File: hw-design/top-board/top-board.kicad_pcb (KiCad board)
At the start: 2 copper layers, 170 x 65.9 mm, 115 parts, among them P1 POWER_CONN, P2 BACKLIGHT, P3 BACKLIGHT, P4 BOTTOM_CONN, P5 ISP, P6 SPI_JTAG, P7 FOOTSWITCH, P8 FOOTSWITCH, Q1 2N7002, Q2 2N7002, SW1 SW_PUSH, U1 NCP1117DT33G, U2 74AHC1G00, U3 LPC1759FBD80, U4 PCA9685, Y1 10MHz

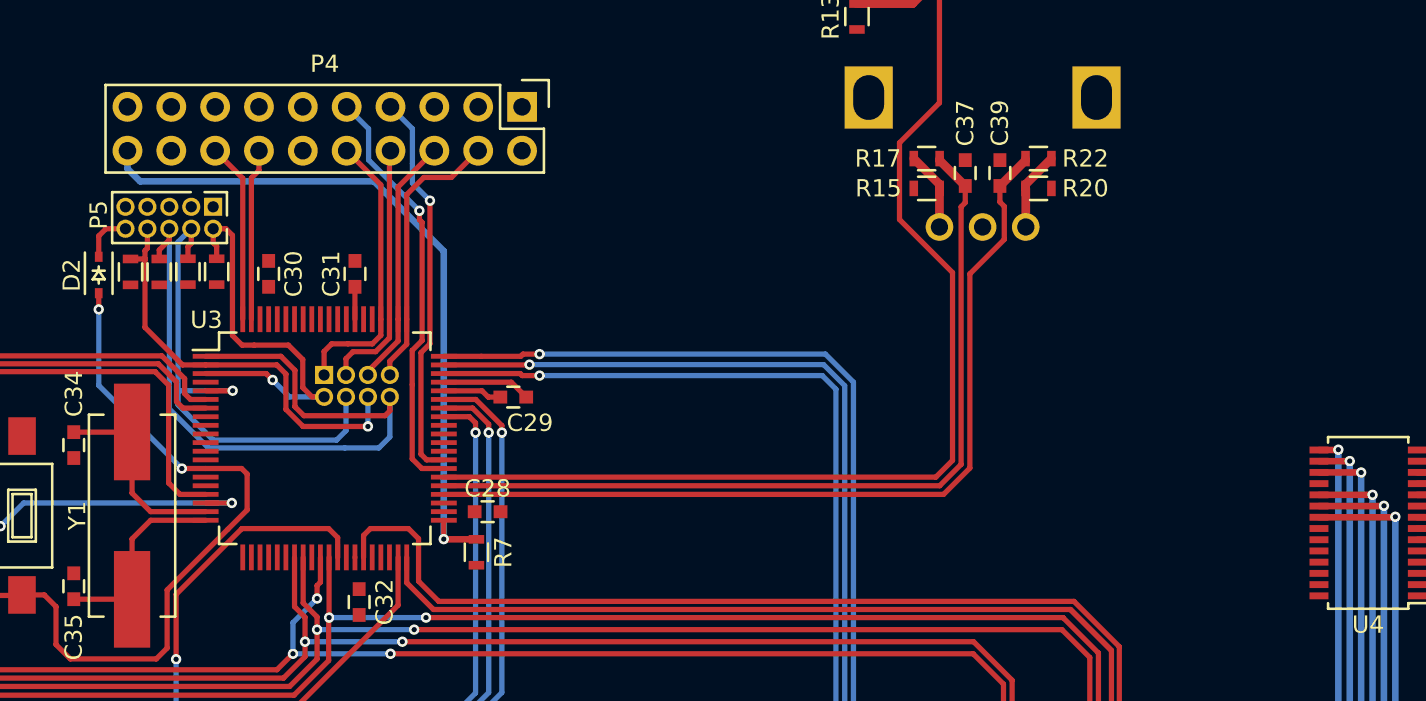
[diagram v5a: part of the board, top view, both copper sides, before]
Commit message: pcb,top-board: PCA interface signals traced
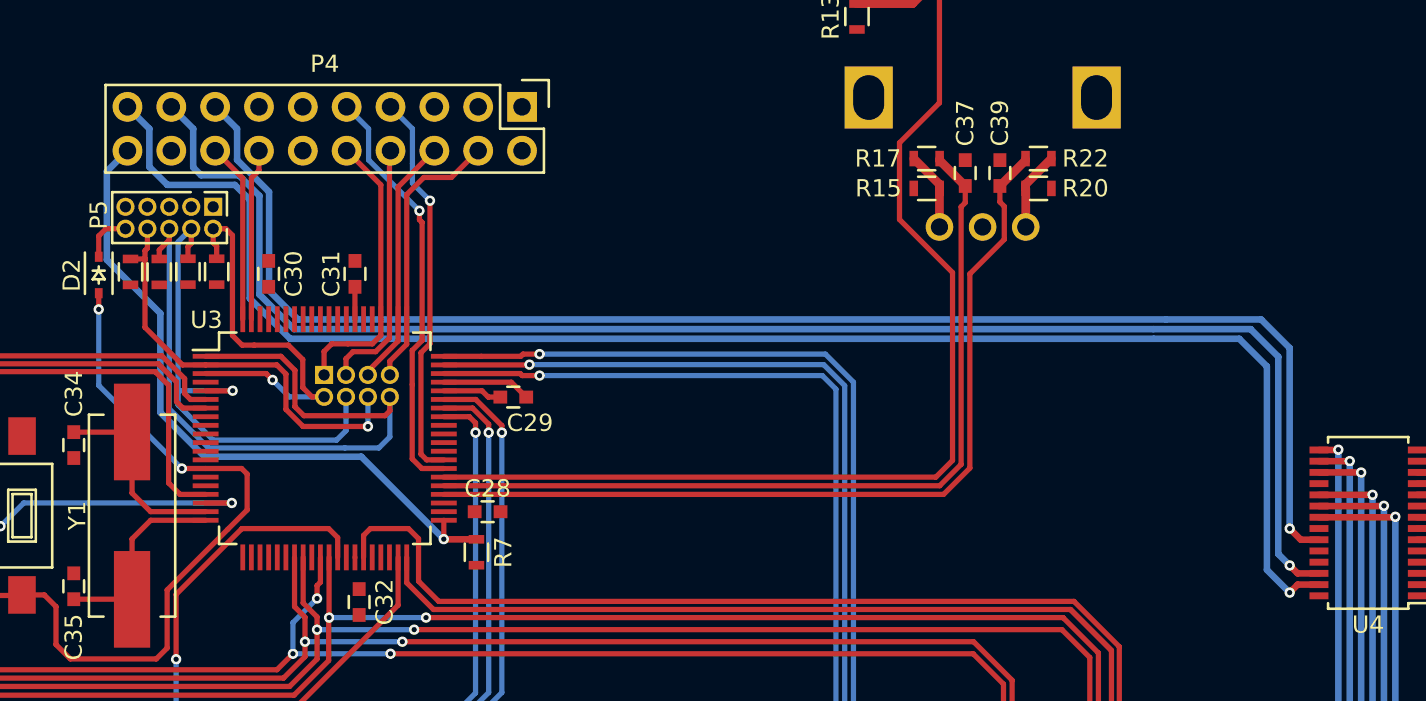
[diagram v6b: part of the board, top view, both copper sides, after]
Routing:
- net PM_LEDS_SDA: track 0.00 -> 92.4 mm, vias 0 -> 1
- net PM_LEDS_SCL: track 0.00 -> 89.0 mm, vias 0 -> 1
- net PM_LEDS_OE: track 0.00 -> 84.9 mm, vias 0 -> 1
- net HMI_ISP_ENABLE: track 41.0 -> 39.4 mm
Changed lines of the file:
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@@
   (general
     (links 318)
-    (no_connects 163)
+    (no_connects 160)
     (area 71.624905 39.007697 241.724909 105.045908)
     (thickness 1.6)
     (drawings 9)
-    (tracks 709)
+    (tracks 753)
     (zones 0)
     (modules 115)
@@
   )
   (setup
-    (last_trace_width 0.3048)
+    (last_trace_width 0.381)
     (user_trace_width 0.2032)
     (user_trace_width 0.254)
@@
   (gr_line (start 241.674908 39.057698) (end 71.674906 39.057698) (layer Edge.Cuts) (width 0.1))
   (gr_line (start 71.674906 104.995907) (end 241.674908 104.995907) (layer Edge.Cuts) (width 0.1))
-  (segment (start 163.5926 64.7204) (end 167.5022 64.7204) (width 0.3048) (layer F.Cu) (net 2) (status 400000))
-  (segment (start 167.5022 64.7204) (end 168.3646 65.5828) (width 0.3048) (layer F.Cu) (net 2) (status 800000))
-  (segment (start 166.8646 65.5828) (end 166.1668 65.5828) (width 0.3048) (layer F.Cu) (net 3) (status 400000))
+  (segment (start 163.5926 64.7204) (end 167.5022 64.7204) (width 0.3048) (layer F.Cu) (net 2))
+  (segment (start 167.5022 64.7204) (end 168.3646 65.5828) (width 0.3048) (layer F.Cu) (net 2))
+  (segment (start 166.8646 65.5828) (end 166.1668 65.5828) (width 0.3048) (layer F.Cu) (net 3))
   (segment (start 166.1668 65.5828) (end 165.8044 65.2204) (width 0.3048) (layer F.Cu) (net 3))
-  (segment (start 163.5926 65.2204) (end 165.8044 65.2204) (width 0.3048) (layer F.Cu) (net 3) (status 400000))
+  (segment (start 163.5926 65.2204) (end 165.8044 65.2204) (width 0.3048) (layer F.Cu) (net 3))
   (segment (start 158.4426 59.198) (end 158.4452 59.1954) (width 0.3048) (layer F.Cu) (net 3))
   (segment (start 158.4426 61.0704) (end 158.4426 59.198) (width 0.3048) (layer F.Cu) (net 3))
@@
   (segment (start 152.8826 52.451) (end 152.8826 51.308) (width 0.3048) (layer F.Cu) (net 78))
   (segment (start 152.4426 61.0704) (end 152.4426 52.891) (width 0.3048) (layer F.Cu) (net 78))
+  (segment (start 214.2946 73.8476) (end 213.2428 73.8476) (width 0.381) (layer F.Cu) (net 79) (status 400000))
+  (segment (start 210.947 61.087) (end 205.4352 61.087) (width 0.381) (layer B.Cu) (net 79))
+  (segment (start 212.598 62.738) (end 210.947 61.087) (width 0.381) (layer B.Cu) (net 79))
+  (segment (start 212.598 73.2028) (end 212.598 62.738) (width 0.381) (layer B.Cu) (net 79))
+  (via (at 212.598 73.2028) (size 0.6) (layers F.Cu B.Cu) (net 79))
+  (segment (start 213.2428 73.8476) (end 212.598 73.2028) (width 0.381) (layer F.Cu) (net 79))
+  (segment (start 150.3426 48.768) (end 151.6126 50.038) (width 0.381) (layer B.Cu) (net 79) (status 400000))
+  (segment (start 155.1432 61.087) (end 205.4352 61.087) (width 0.381) (layer B.Cu) (net 79))
+  (segment (start 153.4668 59.4106) (end 155.1432 61.087) (width 0.381) (layer B.Cu) (net 79))
+  (segment (start 153.4668 53.6956) (end 153.4668 59.4106) (width 0.381) (layer B.Cu) (net 79))
+  (segment (start 151.6126 51.8414) (end 153.4668 53.6956) (width 0.381) (layer B.Cu) (net 79))
+  (segment (start 151.6126 50.038) (end 151.6126 51.8414) (width 0.381) (layer B.Cu) (net 79))
   (segment (start 151.9426 52.908) (end 150.3426 51.308) (width 0.3048) (layer F.Cu) (net 80))
   (segment (start 151.9426 61.0704) (end 151.9426 52.908) (width 0.3048) (layer F.Cu) (net 80))
-  (segment (start 145.2626 52.3494) (end 145.9992 53.086) (width 0.381) (layer B.Cu) (net 84))
-  (segment (start 145.9992 53.086) (end 159.5501 53.086) (width 0.381) (layer B.Cu) (net 84))
-  (segment (start 159.5501 53.086) (end 163.5887 57.1246) (width 0.381) (layer B.Cu) (net 84))
-  (segment (start 163.5887 57.1246) (end 163.5887 73.8124) (width 0.381) (layer B.Cu) (net 84))
+  (segment (start 214.2946 75.7976) (end 213.0592 75.7976) (width 0.381) (layer F.Cu) (net 81) (status 400000))
+  (segment (start 210.3374 61.6458) (end 204.6986 61.6458) (width 0.381) (layer B.Cu) (net 81))
+  (segment (start 211.9376 63.246) (end 210.3374 61.6458) (width 0.381) (layer B.Cu) (net 81))
+  (segment (start 211.9376 74.676) (end 211.9376 63.246) (width 0.381) (layer B.Cu) (net 81))
+  (segment (start 212.598 75.3364) (end 211.9376 74.676) (width 0.381) (layer B.Cu) (net 81))
+  (via (at 212.598 75.3364) (size 0.6) (layers F.Cu B.Cu) (net 81))
+  (segment (start 213.0592 75.7976) (end 212.598 75.3364) (width 0.381) (layer F.Cu) (net 81))
+  (segment (start 147.8026 48.768) (end 149.0726 50.038) (width 0.381) (layer B.Cu) (net 81) (status 400000))
+  (segment (start 154.9146 61.6458) (end 204.6986 61.6458) (width 0.381) (layer B.Cu) (net 81))
+  (segment (start 152.908 59.6392) (end 154.9146 61.6458) (width 0.381) (layer B.Cu) (net 81))
+  (segment (start 152.908 53.9242) (end 152.908 59.6392) (width 0.381) (layer B.Cu) (net 81))
+  (segment (start 151.7142 52.7304) (end 152.908 53.9242) (width 0.381) (layer B.Cu) (net 81))
+  (segment (start 149.527402 52.7304) (end 151.7142 52.7304) (width 0.381) (layer B.Cu) (net 81))
+  (segment (start 149.0726 52.275598) (end 149.527402 52.7304) (width 0.381) (layer B.Cu) (net 81))
+  (segment (start 149.0726 50.038) (end 149.0726 52.275598) (width 0.381) (layer B.Cu) (net 81))
+  (segment (start 214.2946 76.4476) (end 213.0616 76.4476) (width 0.381) (layer F.Cu) (net 83) (status 400000))
+  (segment (start 209.677 62.2046) (end 204.724 62.2046) (width 0.381) (layer B.Cu) (net 83))
+  (segment (start 211.2772 63.8048) (end 209.677 62.2046) (width 0.381) (layer B.Cu) (net 83))
+  (segment (start 211.2772 75.5904) (end 211.2772 63.8048) (width 0.381) (layer B.Cu) (net 83))
+  (segment (start 212.598 76.9112) (end 211.2772 75.5904) (width 0.381) (layer B.Cu) (net 83))
+  (via (at 212.598 76.9112) (size 0.6) (layers F.Cu B.Cu) (net 83))
+  (segment (start 213.0616 76.4476) (end 212.598 76.9112) (width 0.381) (layer F.Cu) (net 83))
+  (segment (start 145.2626 48.768) (end 146.5326 50.038) (width 0.381) (layer B.Cu) (net 83) (status 400000))
+  (segment (start 154.686 62.2046) (end 204.724 62.2046) (width 0.381) (layer B.Cu) (net 83))
+  (segment (start 152.3492 59.8678) (end 154.686 62.2046) (width 0.381) (layer B.Cu) (net 83))
+  (segment (start 152.3492 54.1528) (end 152.3492 59.8678) (width 0.381) (layer B.Cu) (net 83))
+  (segment (start 151.4856 53.2892) (end 152.3492 54.1528) (width 0.381) (layer B.Cu) (net 83))
+  (segment (start 147.574 53.2892) (end 151.4856 53.2892) (width 0.381) (layer B.Cu) (net 83))
+  (segment (start 146.5326 52.2478) (end 147.574 53.2892) (width 0.381) (layer B.Cu) (net 83))
+  (segment (start 146.5326 50.038) (end 146.5326 52.2478) (width 0.381) (layer B.Cu) (net 83))
+  (segment (start 145.2626 51.308) (end 144.0688 52.5018) (width 0.381) (layer B.Cu) (net 84) (status 400000))
+  (segment (start 158.8135 69.0372) (end 163.5887 73.8124) (width 0.381) (layer B.Cu) (net 84))
+  (segment (start 149.733 69.0372) (end 158.8135 69.0372) (width 0.381) (layer B.Cu) (net 84))
+  (segment (start 147.1676 66.4718) (end 149.733 69.0372) (width 0.381) (layer B.Cu) (net 84))
+  (segment (start 147.1676 60.7314) (end 147.1676 66.4718) (width 0.381) (layer B.Cu) (net 84))
+  (segment (start 144.0688 57.6326) (end 147.1676 60.7314) (width 0.381) (layer B.Cu) (net 84))
+  (segment (start 144.0688 52.5018) (end 144.0688 57.6326) (width 0.381) (layer B.Cu) (net 84))
   (via (at 163.5887 73.8124) (size 0.6) (layers F.Cu B.Cu) (net 84))
   (segment (start 163.5887 73.8124) (end 163.6007 73.8244) (width 0.381) (layer F.Cu) (net 84))
   (segment (start 163.6007 73.8244) (end 165.481 73.8244) (width 0.381) (layer F.Cu) (net 84))
-  (segment (start 145.2626 51.308) (end 145.2626 52.3494) (width 0.381) (layer B.Cu) (net 84))
   (segment (start 163.5926 73.8085) (end 163.5887 73.8124) (width 0.3048) (layer F.Cu) (net 84))
   (segment (start 163.5926 72.7204) (end 163.5926 73.8085) (width 0.3048) (layer F.Cu) (net 84))

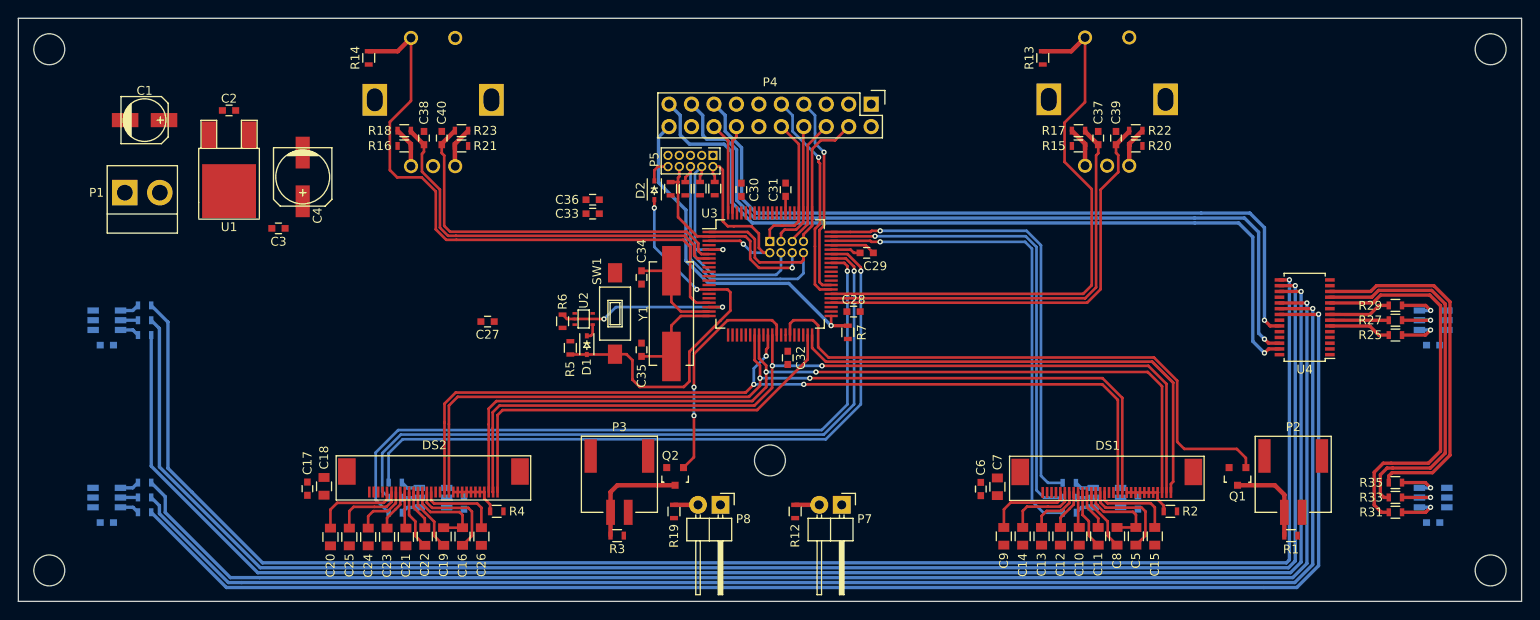
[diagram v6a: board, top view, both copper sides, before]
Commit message: pcb,top-board: added top layer cupper zone
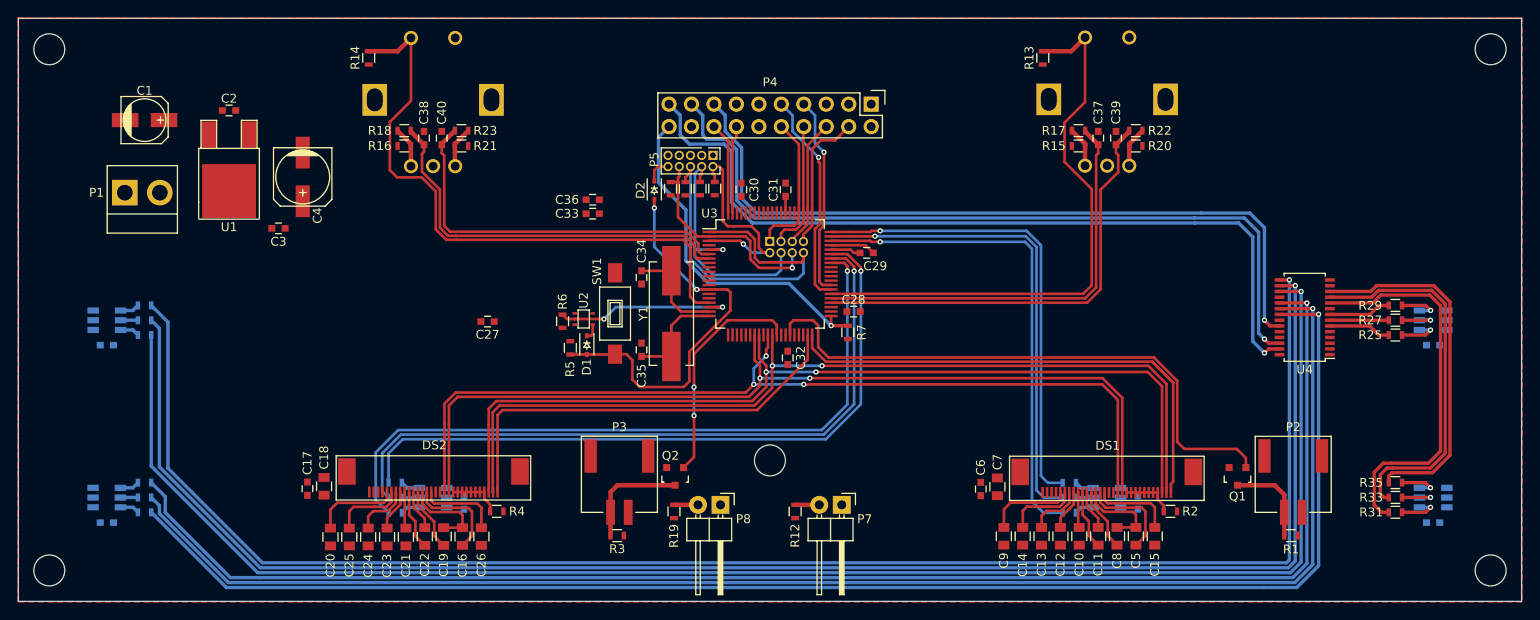
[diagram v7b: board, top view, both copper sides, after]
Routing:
- added copper zone on F.Cu, net GNDD
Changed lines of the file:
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@@
   (general
     (links 318)
-    (no_connects 160)
+    (no_connects 112)
     (area 71.624905 39.007697 241.724909 105.045908)
     (thickness 1.6)
@@
   (segment (start 86.7036 94.9198) (end 95.2126 103.4288) (width 0.381) (layer B.Cu) (net 113))
   (segment (start 95.2126 103.4288) (end 212.5218 103.4288) (width 0.381) (layer B.Cu) (net 113))
+  (zone (net 2) (net_name GNDD) (layer F.Cu) (hatch edge 0.508)
+    (connect_pads (clearance 0.508))
+    (min_thickness 0.254)
+    (fill yes (arc_segments 16) (thermal_gap 0.508) (thermal_bridge_width 0.508))
+    (polygon
+      (pts
+        (xy 71.6026 38.989) (xy 241.7572 38.989) (xy 241.7572 105.0798) (xy 71.6026 105.0798)
+      )
+    )
+  )
 )

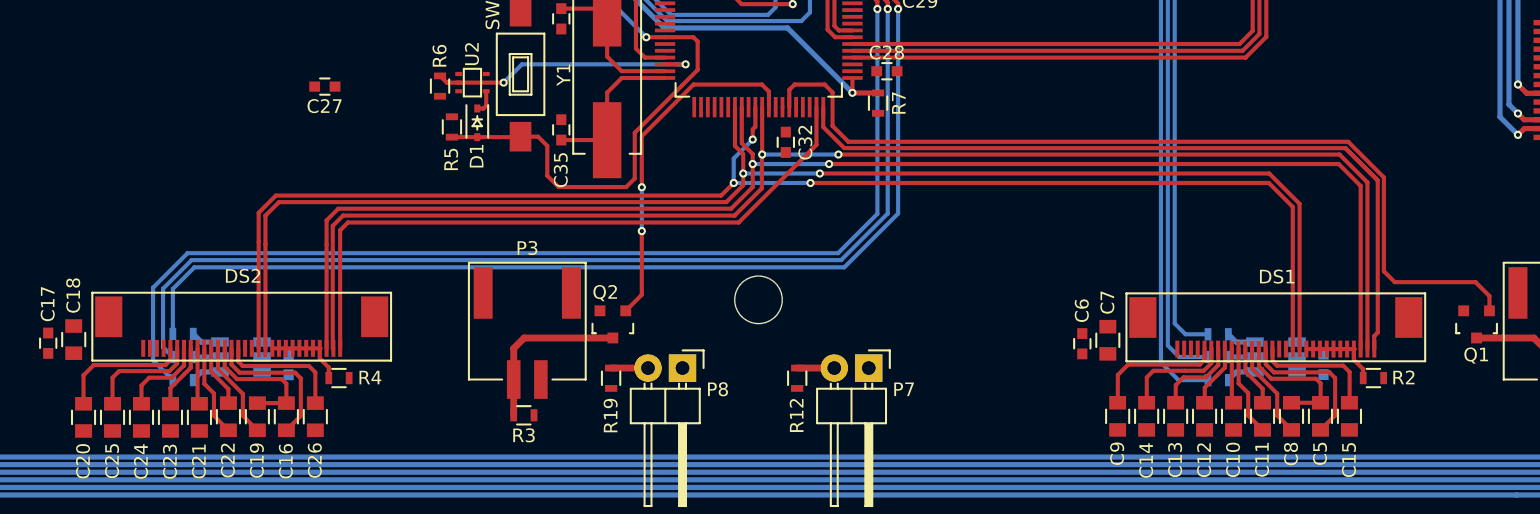
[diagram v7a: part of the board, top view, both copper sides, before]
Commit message: pcb,top-board: some traces improvement
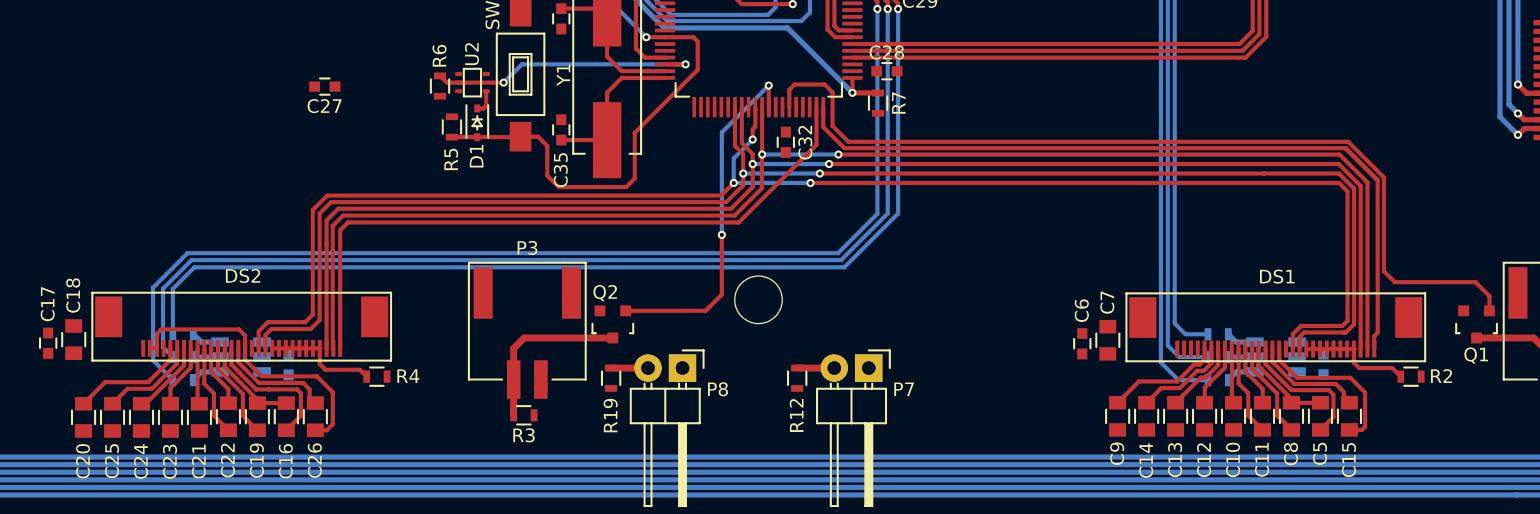
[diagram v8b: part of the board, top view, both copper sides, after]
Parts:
- moved R4 2.80 mm to (128.6, 94.7)
- moved R2 2.77 mm to (204.7, 94.7)
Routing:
- net GNDD: track 5.13 -> 38.5 mm
- net GLCD_SCL: track 104.5 -> 112.1 mm
- net GLCD_SI: track 104.5 -> 112.0 mm
- net Net-(C16-Pad2): track 9.97 -> 7.16 mm
- net Net-(C5-Pad2): track 9.97 -> 7.39 mm
- net Net-(DS2-Pad20): track 6.05 -> 8.59 mm
- net Net-(DS1-Pad20): track 6.01 -> 8.47 mm
- net Net-(C9-Pad2): track 9.82 -> 8.58 mm
- net Net-(C20-Pad2): track 9.82 -> 8.59 mm
- net Net-(C15-Pad2): track 9.24 -> 8.09 mm
- net Net-(C14-Pad2): track 8.23 -> 7.09 mm
- net Net-(C25-Pad2): track 8.23 -> 7.10 mm
- net Net-(C26-Pad2): track 9.24 -> 8.29 mm
- net Net-(C5-Pad1): track 11.0 -> 10.0 mm
- net Net-(C24-Pad2): track 6.34 -> 5.55 mm
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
